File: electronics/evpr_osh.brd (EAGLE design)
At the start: 109.5 x 61.5 mm, 140 parts

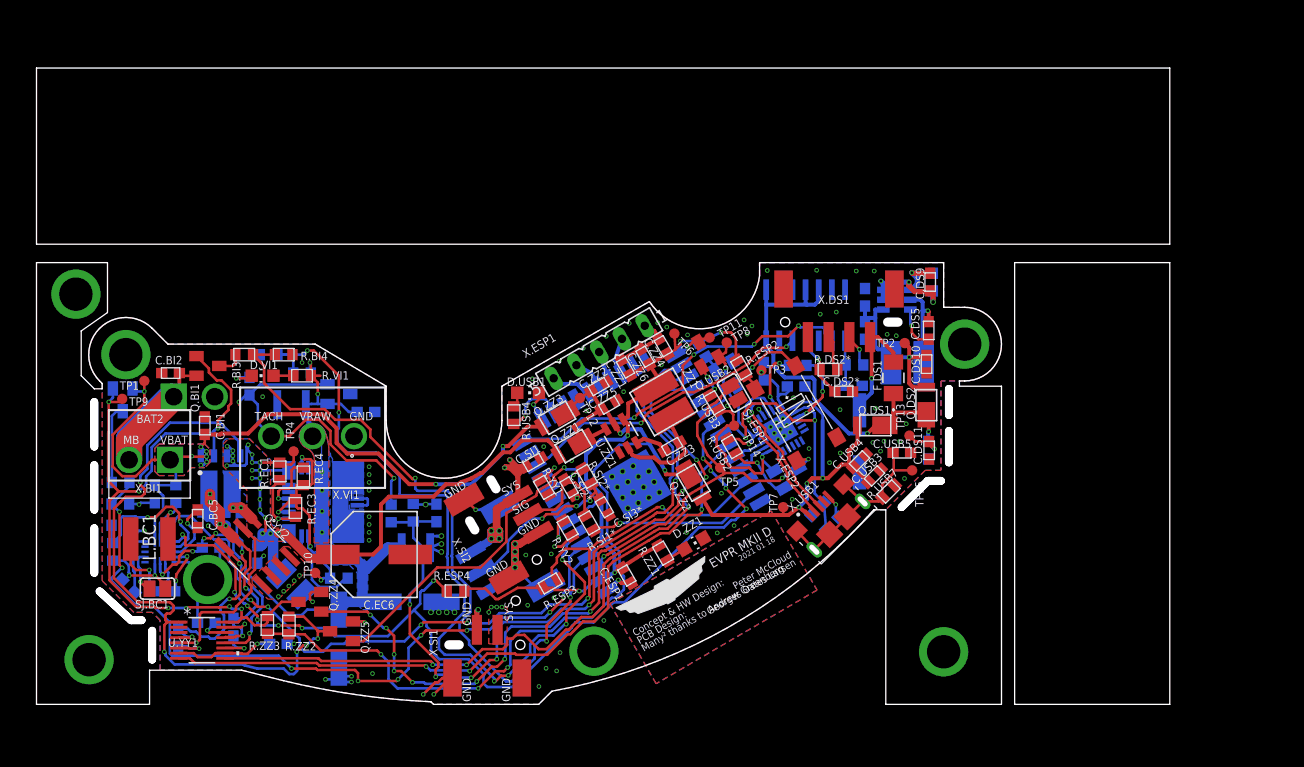
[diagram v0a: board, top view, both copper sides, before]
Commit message: Performed DRC checks, fixed minor issues, redid OSH version
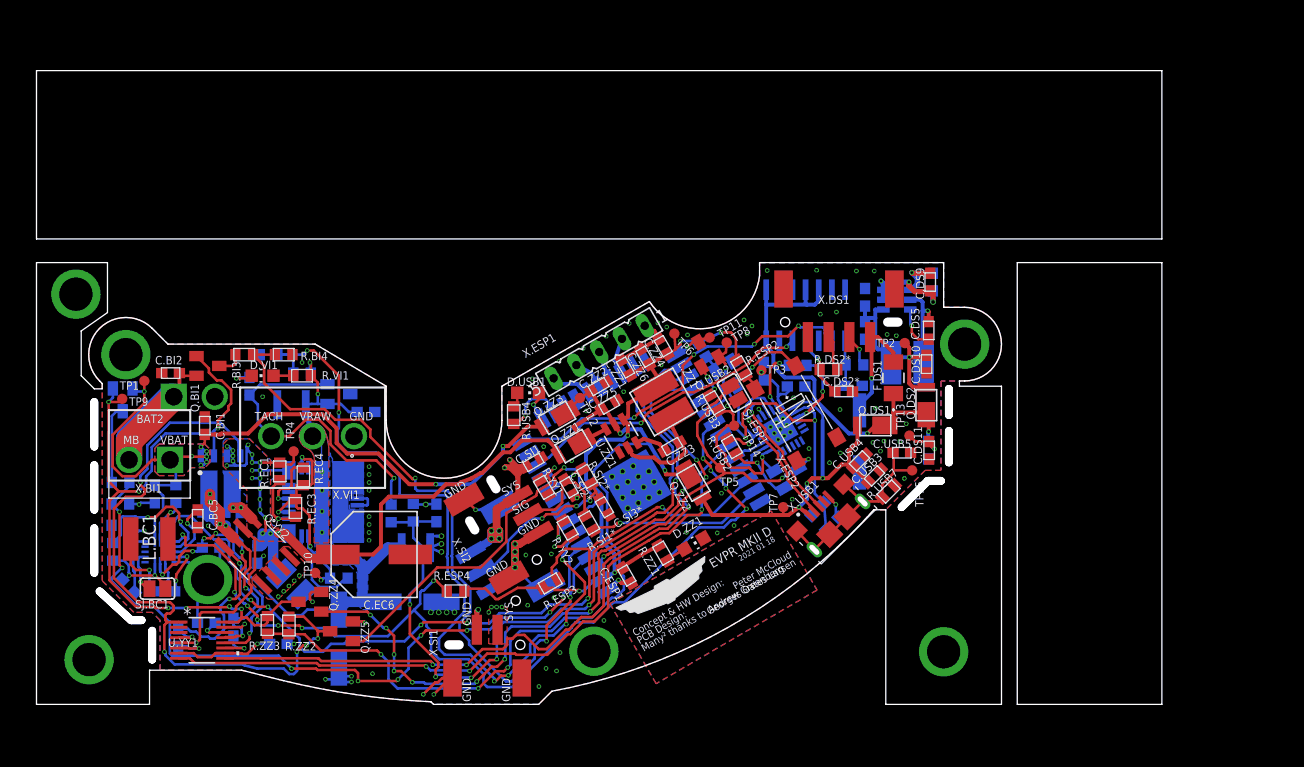
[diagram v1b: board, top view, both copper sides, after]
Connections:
- removed net USING_BAT: U.YY1.9
- net !USING_BAT: now also U.YY1.9
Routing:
- net !USING_BAT: track 0.00 -> 73.4 mm, vias 0 -> 3
- net USING_BAT: track 72.9 -> 0.00 mm, vias 3 -> 0
- net TACH_RAW: track 32.7 -> 31.5 mm, vias 2 -> 1
- net VRAW: track 73.2 -> 72.3 mm
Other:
- board size 109.5 x 61.5 mm -> 108.7 x 61.2 mm

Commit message: add copper to shims
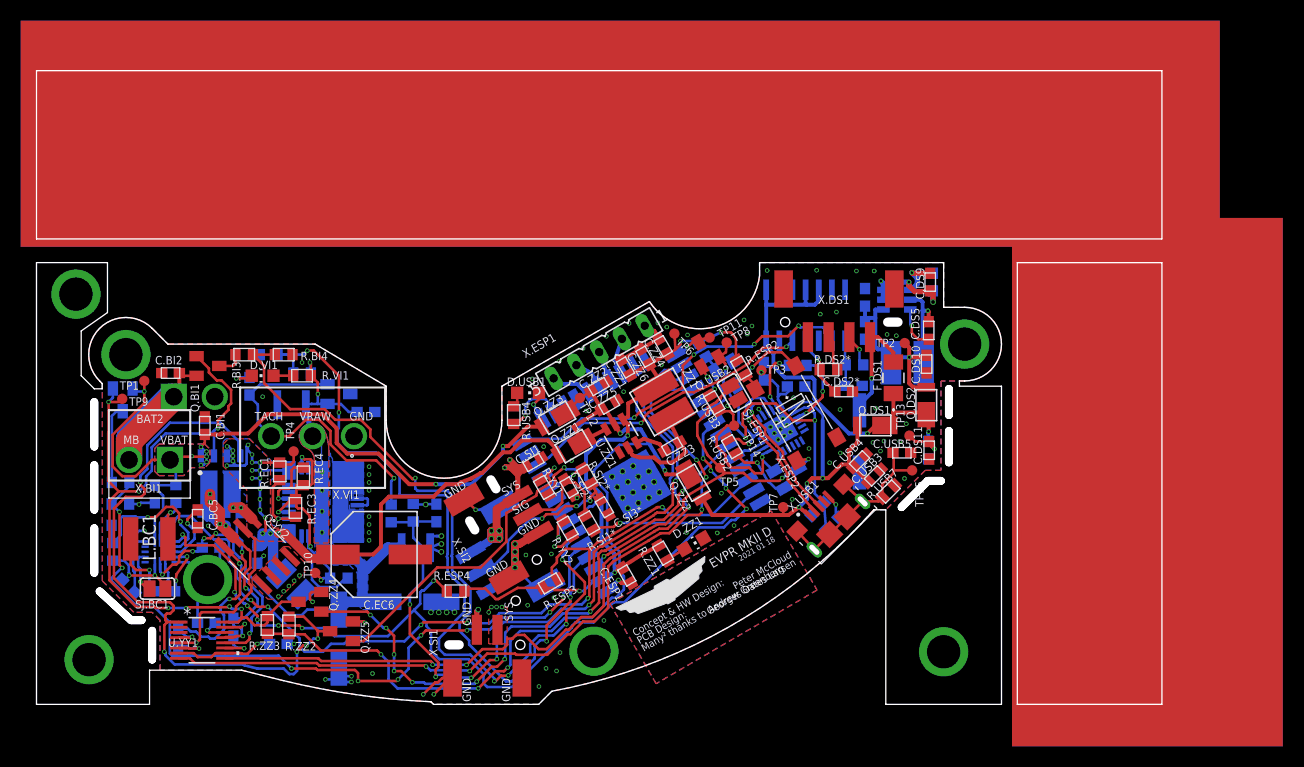
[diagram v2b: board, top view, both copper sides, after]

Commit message: Remove shims from evpr_osh.brd
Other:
- board size 108.7 x 61.2 mm -> 93.2 x 42.7 mm
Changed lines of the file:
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@@
 <text x="9.906" y="-43.434" size="0.8128" layer="22" font="vector" ratio="15" rot="MR330">GND</text>
 <text x="8.128" y="-37.846" size="0.8128" layer="22" font="vector" ratio="15" rot="MR330">GND</text>
-<wire x1="-39.37" y1="-11.176" x2="69.342" y2="-11.176" width="0.0254" layer="20"/>
-<wire x1="69.342" y1="-11.176" x2="69.342" y2="5.08" width="0.0254" layer="20"/>
-<wire x1="69.342" y1="5.08" x2="-39.37" y2="5.08" width="0.0254" layer="20"/>
-<wire x1="-39.37" y1="5.08" x2="-39.37" y2="-11.176" width="0.0254" layer="20"/>
-<wire x1="55.372" y1="-13.462" x2="55.372" y2="-56.134" width="0.0254" layer="20"/>
-<wire x1="55.372" y1="-56.134" x2="69.342" y2="-56.134" width="0.0254" layer="20"/>
-<wire x1="69.342" y1="-56.134" x2="69.342" y2="-13.462" width="0.0254" layer="20"/>
-<wire x1="69.342" y1="-13.462" x2="55.372" y2="-13.462" width="0.0254" layer="20"/>
 <rectangle x1="-40.894" y1="-12.192" x2="74.93" y2="9.652" layer="2"/>
-<rectangle x1="54.864" y1="-60.198" x2="81.026" y2="-9.144" layer="16"/>
 <rectangle x1="-40.894" y1="-11.938" x2="74.93" y2="9.906" layer="15"/>
-<rectangle x1="54.864" y1="-60.198" x2="81.026" y2="-9.144" layer="1"/>
 <rectangle x1="54.864" y1="-60.452" x2="81.026" y2="-9.398" layer="15"/>
 <rectangle x1="54.61" y1="-60.198" x2="80.772" y2="-9.144" layer="2"/>
-<rectangle x1="-40.894" y1="-11.938" x2="74.93" y2="9.906" layer="1"/>
-<rectangle x1="-40.894" y1="-11.938" x2="74.93" y2="9.906" layer="16"/>
 </plain>
 <attributes>

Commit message: Update osh version
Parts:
- removed C.USB1, C.USB4: 4.7uF, mccloud:C0603
- removed C.USB2, C.USB3: 0.1uF, mccloud:C0603
- removed C.USB5: 4.7 nF, mccloud:C0603
- removed Q.ESP1: DMN5L06K-7, mccloud:SOT23
- removed Q.USB1, Q.USB2: MMBT2222A, transistor-neu-to92:SOT23-BEC
- removed R.ESP1, R.USB2, R.USB3: 10k, mccloud:R0603
- removed R.USB1: 1k, mccloud:R0603
- removed R.USB5: 22.1k, mccloud:R0603
- removed R.USB6: 47.5K, mccloud:R0603
- removed R.USB7: 1M, mccloud:R0603
- removed SJ.ESP1: (no value), jumper:SJ
- removed TP11, TP14, TP15, TP3, TP5, TP7, TP8: PTR1TP10R, testpad:TP10R
- removed U.USB1: CP2102N-A02-GQFN24R, mccloud:QFN24-4X4
- removed X.ESP2: RSTBTN, mccloud:PTS645
- removed X.USB1: 10118193-0001LF, mccloud:FCI_10118193-0001LF
- added SV1: PR20B04HBDN, mccloud:PR20B04HBDN
- moved C.DS1 7.55 mm to (33.2, -27.7), turned to 60 degrees
- moved R.ESP2 3.94 mm to (27.7, -27.4)
- moved C.ESP1 0.84 mm to (18.3, -43.2)
- moved C.SI3* 0.76 mm to (16.2, -36.7)
- moved R.SI1* 0.64 mm to (14.7, -38.6)
- moved R.SI2* 0.56 mm to (14.4, -33.9)
- moved Q.ZZ3 0.54 mm to (11.0, -27.9)
- moved C.DS4* 0.23 mm to (39.8, -25.4)
- moved Q.ZZ1 0.08 mm to (12.6, -31.2)
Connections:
- removed net N$1: Q.ESP1.3, X.ESP2.P$1, X.ESP2.P$2
- removed net N$16: R.USB1.1, U.USB1.9
- removed net N$18: Q.USB1.E, R.USB3.2, TP14.TP, U.USB1.19
- removed net N$19: Q.USB2.E, R.USB2.2, TP8.TP, U.USB1.23
- removed net N$20: Q.USB1.B, R.USB2.1
- removed net N$21: Q.USB2.B, R.USB3.1
- removed net N$34: C.USB5.2, R.USB7.2, TP15.TP, X.USB1.S1, X.USB1.S2, X.USB1.S3, X.USB1.S4, X.USB1.S5, X.USB1.S6
- removed net N$39: R.USB1.2, U.USB1.5
- removed net N$40: C.USB1.2, C.USB2.2, TP3.TP, U.USB1.6
- removed net RST_DISABLE: Q.ESP1.1, R.ESP1.2, U.ESP1.30
- removed net USBD+: U.USB1.3, X.USB1.3
- removed net USBD-: U.USB1.4, X.USB1.2
- removed net USBSENSE: R.USB5.1, R.USB6.2, U.ESP1.32, U.USB1.8
- removed net VUSB: C.USB3.2, C.USB4.2, Q.DS1.A, Q.ZZ2.A, R.USB5.2, TP7.TP, U.USB1.7, X.USB1.1
- new net VPROG: Q.DS1.A, Q.ZZ2.A, SV1.P$6
- net BOOTMODE: now also SV1.P$3; no longer Q.USB2.C, TP11.TP
- net ESP_POWER: now also SV1.P$8; no longer R.ESP1.1
- net ESP_RX: now also SV1.P$5; no longer U.USB1.21
- net ESP_TX: now also SV1.P$7; no longer U.USB1.20
- net GND: now also SV1.P$2; no longer C.USB1.1, C.USB2.1, C.USB3.1, C.USB4.1, C.USB5.1, Q.ESP1.2, R.USB6.1, R.USB7.1, SJ.ESP1.1, U.USB1.2, U.USB1.EXP, X.USB1.5
- net RESET: now also SV1.P$1; no longer Q.USB1.C, SJ.ESP1.2, TP5.TP, X.ESP2.P$3, X.ESP2.P$4
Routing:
- net VUSB: track 38.4 -> 0.00 mm, vias 3 -> 0
- net USBSENSE: track 27.4 -> 0.00 mm, vias 2 -> 0
- net VPROG: track 0.00 -> 26.9 mm
- net BOOTMODE: track 3.97 -> 28.4 mm, vias 1 -> 2
- net N$34: track 20.2 -> 0.00 mm
- net USBD-: track 16.3 -> 0.00 mm, vias 1 -> 0
- net N$18: track 16.1 -> 0.00 mm, vias 1 -> 0
- net N$19: track 14.8 -> 0.00 mm, vias 2 -> 0
- net ESP_POWER: track 63.6 -> 78.1 mm
- net USBD+: track 14.3 -> 0.00 mm, vias 1 -> 0
- net ESP_TX: track 3.57 -> 17.2 mm
- net ESP_RX: track 3.31 -> 15.8 mm
- net RESET: track 40.7 -> 30.6 mm, vias 3 -> 1
- net N$1: track 7.80 -> 0.00 mm, vias 1 -> 0
- net N$16: track 7.38 -> 0.00 mm, vias 2 -> 0
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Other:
- board text added: "2021 07 16"
- board text added: "EVPR MKII E"
- board text removed: "2021 01 18"
- board text removed: "EVPR MKII D"

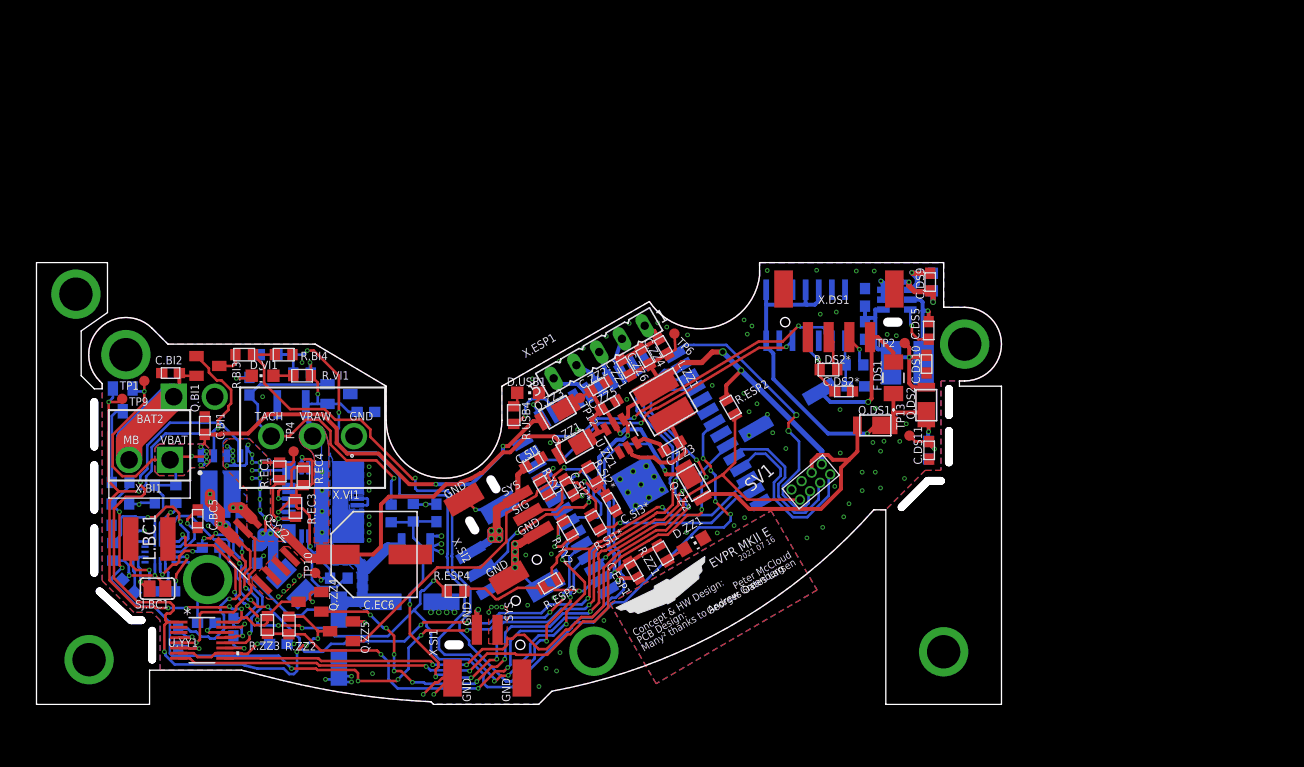
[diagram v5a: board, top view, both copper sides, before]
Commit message: Various connector changes and other miscellany
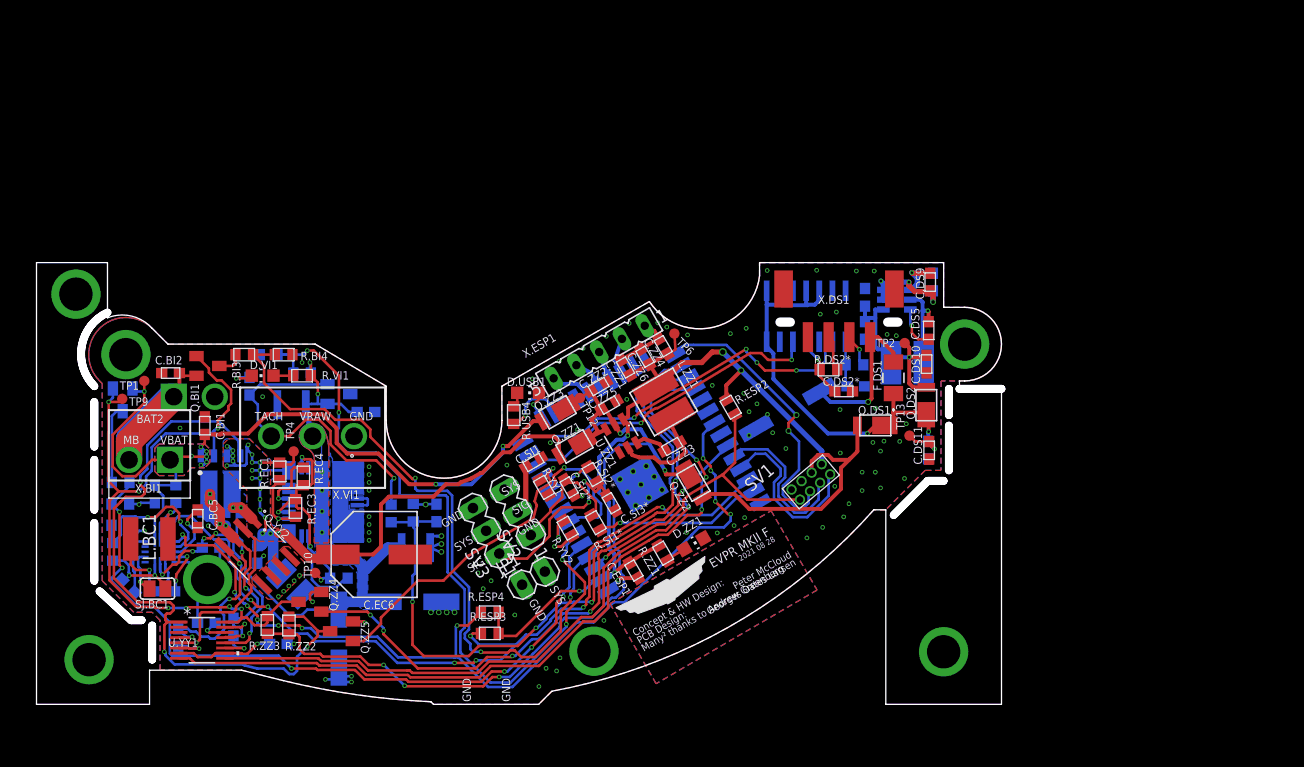
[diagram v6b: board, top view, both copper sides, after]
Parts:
- removed X.SI1: BM02B-PASS-1-TFT(LF)(SN), mccloud:BM02B-PASS-1-TFT(LF)(SN)
- removed X.SI2, X.SI3: BM03B-PASS-1-TFT(LF)(SN), mccloud:BM03B-PASS-1-TFT(LF)(SN)
- added JP1: (no value), pinhead:1X02
- added SV2, SV3: (no value), con-lstb:MA03-1
- moved R.ESP3 7.58 mm to (4.42, -49.3), turned to 180 degrees
- moved R.ESP4 3.88 mm to (4.42, -47.2)
- moved U.DS1 0.11 mm to (35.0, -18.6)
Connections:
- net GND: now also JP1.1, SV2.3, SV3.3; no longer X.SI1.P$1, X.SI1.P$5, X.SI1.P$6, X.SI2.P$3, X.SI2.P$5, X.SI2.P$6, X.SI3.P$3, X.SI3.P$5, X.SI3.P$6
- net N$11: now also SV2.1; no longer X.SI2.P$2
- net N$12: now also SV3.1; no longer X.SI3.P$2
- net SYS_POWER: now also JP1.2, SV2.2, SV3.2; no longer X.SI1.P$2, X.SI2.P$1, X.SI3.P$1
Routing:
- net GND: track 99.9 -> 72.7 mm, vias 120 -> 112
- net SYS_POWER: track 38.3 -> 26.7 mm, vias 18 -> 10
- net TACH: track 72.6 -> 67.4 mm, vias 6 -> 4
- net BAT_EN: track 58.2 -> 54.0 mm, vias 9 -> 5
- net !ACOK: track 90.2 -> 86.6 mm
- net RAWSENSE: track 74.4 -> 71.2 mm, vias 6 -> 4
- net BATSENSE2: track 66.4 -> 63.7 mm
- net N$9: track 85.7 -> 84.1 mm
- net DS_DAT: track 29.1 -> 30.7 mm
- net N$12: track 19.7 -> 18.2 mm, vias 3 -> 2
- net DS_CLK: track 34.5 -> 35.7 mm, vias 2 -> 4
- net !USING_BAT: track 73.3 -> 72.4 mm, vias 3 -> 1
- net N$11: track 11.4 -> 12.1 mm
- net BATSENSE1: track 71.4 -> 70.8 mm, vias 9 -> 6
- net !USING_ENG: track 77.1 -> 77.5 mm, vias 5 -> 3
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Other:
- outline, holes or cut-outs redrawn
- board text added: "2021 08 28"
- board text added: "EVPR MKII F"
- board text removed: "2021 07 16"
- board text removed: "EVPR MKII E"
